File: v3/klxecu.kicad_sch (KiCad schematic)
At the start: 14 parts, among them J1 cam_sensor, J2 Conn_01x06, U1 S36B-WPZK-A, U2 LM2940S-5.0/NOPB, U3 Arduino Mega 2560 Pro

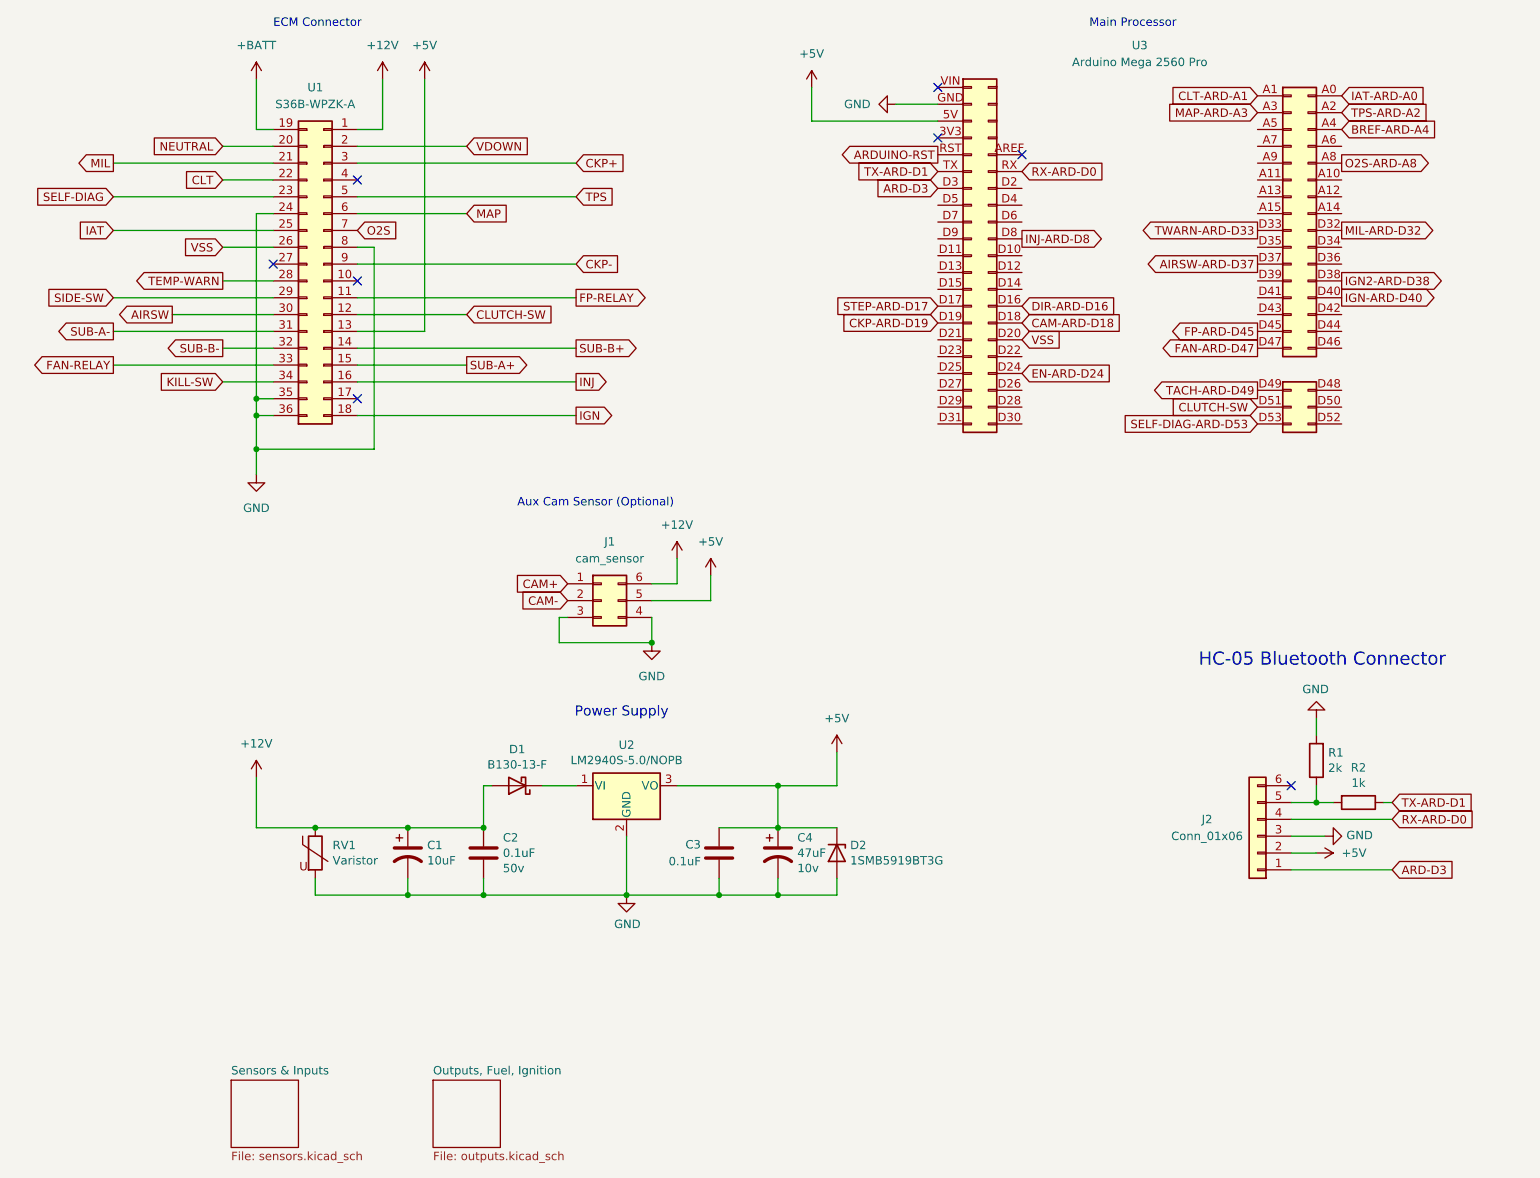
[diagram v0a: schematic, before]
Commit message: change kill switch circuitry
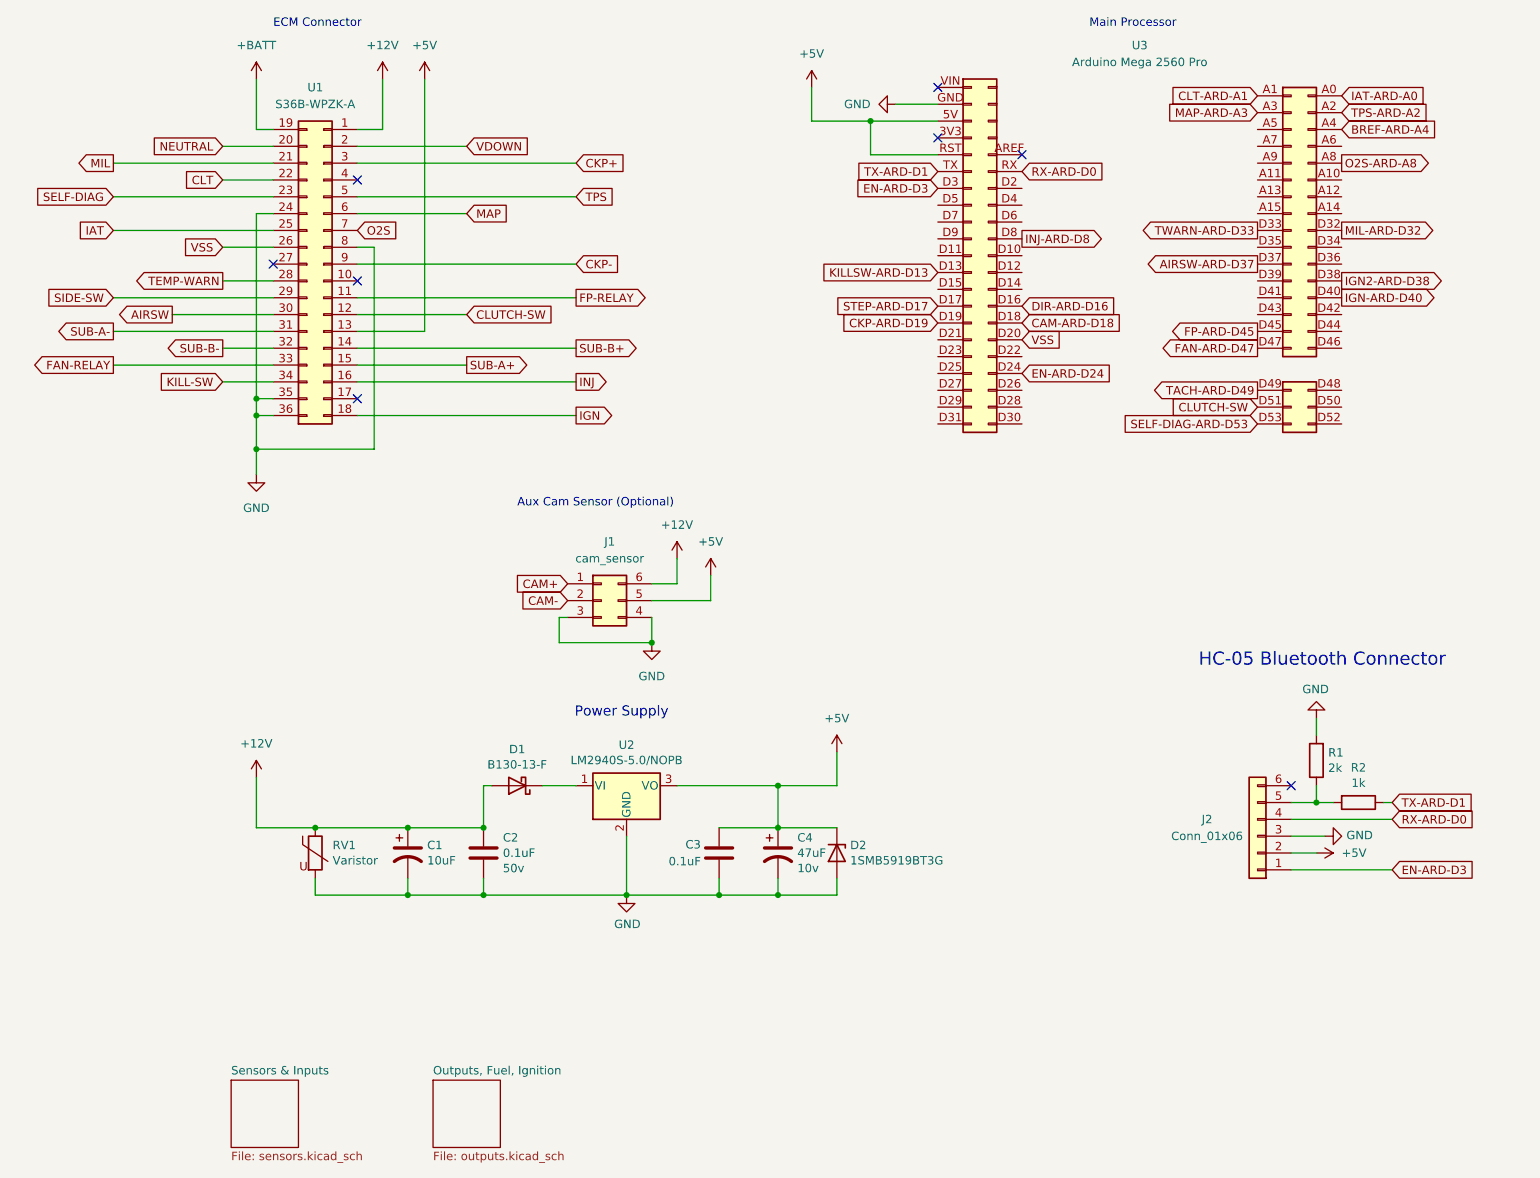
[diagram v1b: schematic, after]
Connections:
- net ARDUINO-RST is gone; now on net +5V: U3.RST
- net KILLSW-ARD-D13: now reaches U3.D13
- net ARD-D3 renamed EN-ARD-D3
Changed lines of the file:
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@@
   (junction (at 215.9 134.62) (diameter 0) (color 0 0 0 0)
+  )
+  (junction (at 148.59 31.75) (diameter 0) (color 0 0 0 0)
   )
   (junction (at 78.74 148.59) (diameter 0) (color 0 0 0 0)
@@
     (stroke (width 0) (type default) (color 0 0 0 0))
   )
-  (wire (pts (xy 139.7 31.75) (xy 158.75 31.75))
+  (wire (pts (xy 139.7 31.75) (xy 148.59 31.75))
     (stroke (width 0) (type default) (color 0 0 0 0))
   )
@@
     (stroke (width 0) (type default) (color 0 0 0 0))
   )
+  (wire (pts (xy 148.59 31.75) (xy 158.75 31.75))
+    (stroke (width 0) (type default) (color 0 0 0 0))
+  )
   (wire (pts (xy 215.9 132.08) (xy 215.9 134.62))
     (stroke (width 0) (type default) (color 0 0 0 0))
@@
     (stroke (width 0) (type default) (color 0 0 0 0))
   )
+  (wire (pts (xy 158.75 36.83) (xy 148.59 36.83))
+    (stroke (width 0) (type default) (color 0 0 0 0))
+  )
   (wire (pts (xy 34.29 38.1) (xy 58.42 38.1))
     (stroke (width 0) (type default) (color 0 0 0 0))
@@
   )
   (wire (pts (xy 71.12 76.2) (xy 104.14 76.2))
+    (stroke (width 0) (type default) (color 0 0 0 0))
+  )
+  (wire (pts (xy 148.59 36.83) (xy 148.59 31.75))
     (stroke (width 0) (type default) (color 0 0 0 0))
   )
@@
     )
   )
-  (global_label "ARD-D3" (shape input) (at 227.33 144.78 0) (fields_autoplaced)
-    (effects (font (size 1.27 1.27)) (justify left))
-    (property "Intersheet References" "${INTERSHEET_REFS}" (id 0) (at 237.4236 144.7006 0)
+  (global_label "EN-ARD-D3" (shape input) (at 227.33 144.78 0) (fields_autoplaced)
+    (effects (font (size 1.27 1.27)) (justify left))
+    (property "Intersheet References" "${INTERSHEET_REFS}" (id 0) (at 241.4755 144.7006 0)
       (effects (font (size 1.27 1.27)) (justify left) hide)
     )
@@
     )
   )
+  (global_label "KILLSW-ARD-D13" (shape input) (at 158.75 54.61 180) (fields_autoplaced)
+    (effects (font (size 1.27 1.27)) (justify right))
+    (property "Intersheet References" "${INTERSHEET_REFS}" (id 0) (at 139.2826 54.5306 0)
+      (effects (font (size 1.27 1.27)) (justify right) hide)
+    )
+  )
   (global_label "MIL-ARD-D32" (shape output) (at 219.71 48.26 0) (fields_autoplaced)
     (effects (font (size 1.27 1.27)) (justify left))
@@
     )
   )
-  (global_label "ARDUINO-RST" (shape output) (at 158.75 36.83 180) (fields_autoplaced)
-    (effects (font (size 1.27 1.27)) (justify right))
-    (property "Intersheet References" "${INTERSHEET_REFS}" (id 0) (at 143.0926 36.9094 0)
-      (effects (font (size 1.27 1.27)) (justify right) hide)
-    )
-  )
   (global_label "FAN-ARD-D47" (shape output) (at 207.01 66.04 180) (fields_autoplaced)
     (effects (font (size 1.27 1.27)) (justify right))
@@
     )
   )
-  (global_label "ARD-D3" (shape input) (at 158.75 41.91 180) (fields_autoplaced)
-    (effects (font (size 1.27 1.27)) (justify right))
-    (property "Intersheet References" "${INTERSHEET_REFS}" (id 0) (at 148.6564 41.9894 0)
+  (global_label "EN-ARD-D3" (shape input) (at 158.75 41.91 180) (fields_autoplaced)
+    (effects (font (size 1.27 1.27)) (justify right))
+    (property "Intersheet References" "${INTERSHEET_REFS}" (id 0) (at 144.6045 41.8306 0)
       (effects (font (size 1.27 1.27)) (justify right) hide)
     )
@@
       (reference "#PWR019") (unit 1) (value "GND") (footprint "")
     )
-    (path "/98f72596-e058-4dba-8464-025a303cdc65/04425876-8a78-41da-a235-fbb98d7c4809"
-      (reference "#PWR020") (unit 1) (value "+5V") (footprint "")
-    )
     (path "/98f72596-e058-4dba-8464-025a303cdc65/4f5864c9-88fd-45df-8336-96f208774aa0"
       (reference "#PWR021") (unit 1) (value "GND") (footprint "")
@@
       (reference "#PWR052") (unit 1) (value "+5V") (footprint "")
     )
+    (path "/98f72596-e058-4dba-8464-025a303cdc65/272dae70-4b24-4de3-9dea-623bc9faa37a"
+      (reference "#PWR053") (unit 1) (value "GND") (footprint "")
+    )
     (path "/a01c941e-2669-451e-92d9-4d3556674fec/75126fec-323d-4a00-8d28-b0141aa312d7"
       (reference "A1") (unit 1) (value "Pololu_Breakout_A4988") (footprint "Module:Pololu_Breakout-16_15.2x20.3mm")
@@
       (reference "JP2") (unit 1) (value "Jumper_2_Open") (footprint "Connector_PinHeader_2.54mm:PinHeader_1x02_P2.54mm_Vertical")
     )
-    (path "/98f72596-e058-4dba-8464-025a303cdc65/769f1426-7971-4738-8ad4-fd6cc8405f3b"
-      (reference "JP3") (unit 1) (value "Jumper_2_Open") (footprint "Jumper:SolderJumper-2_P1.3mm_Open_Pad1.0x1.5mm")
+    (path "/98f72596-e058-4dba-8464-025a303cdc65/5abfb4a7-b746-40aa-8779-e189eca29e83"
+      (reference "JP3") (unit 1) (value "Jumper_3_Open") (footprint "Connector_PinHeader_2.54mm:PinHeader_1x03_P2.54mm_Vertical")
     )
     (path "/a01c941e-2669-451e-92d9-4d3556674fec/a87fbe2b-396d-4f00-a255-233753d9960a"
